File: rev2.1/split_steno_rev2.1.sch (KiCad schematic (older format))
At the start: 59 parts, among them J1 USB_OTG, J2 Audio-Jack-4, J3 Conn_01x03, P1 TC2030-IDC, SW1 SW_Push, SW10 SW_Push, SW11 SW_Push, SW12 SW_Push, SW13 SW_Push, SW14 SW_Push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

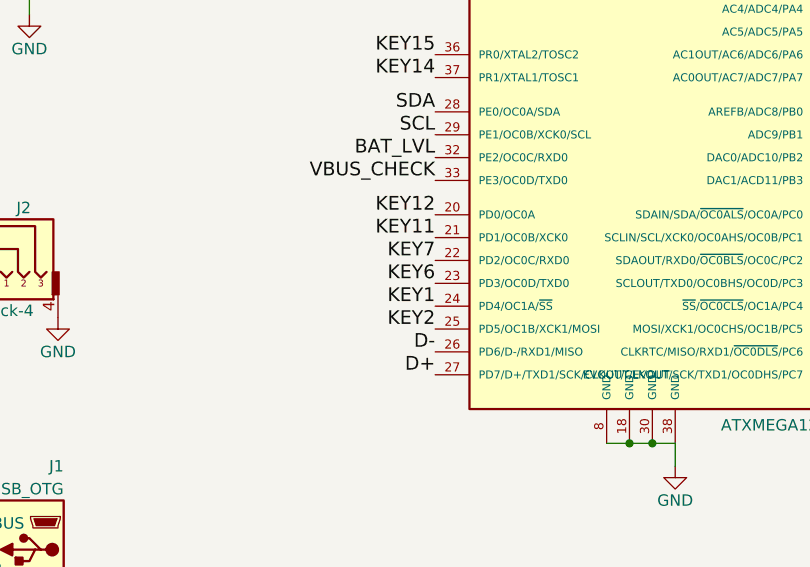
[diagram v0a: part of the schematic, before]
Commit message: routed USB, left side switches
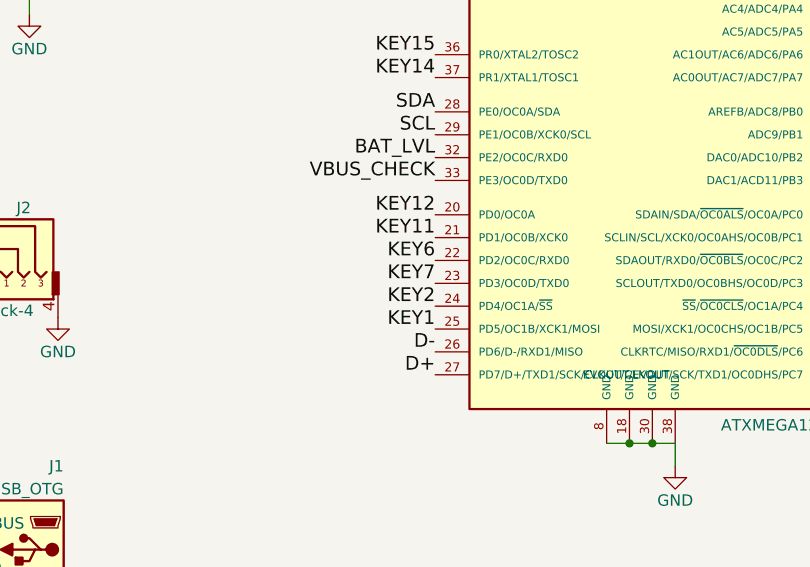
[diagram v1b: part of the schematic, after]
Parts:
- J1: footprint keyboard_parts:USB_miniB -> conn_usb:USB_MicroB_Amphenol_10118194-0001LF
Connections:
- net KEY1: now also U5.25 (PD5/OC1B/XCK1/MOSI); no longer U5.24 (PD4/OC1A/~SS~)
- net KEY2: now also U5.24 (PD4/OC1A/~SS~); no longer U5.25 (PD5/OC1B/XCK1/MOSI)
- net KEY6: now also U5.22 (PD2/OC0C/RXD0); no longer U5.23 (PD3/OC0D/TXD0)
- net KEY7: now also U5.23 (PD3/OC0D/TXD0); no longer U5.22 (PD2/OC0C/RXD0)
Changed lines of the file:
@@
 F 0 "J1" H 6175 7075 50  0000 L CNN
 F 1 "USB_OTG" H 6175 6975 50  0000 L CNN
-F 2 "keyboard_parts:USB_miniB" H 6525 6575 50  0001 C CNN
+F 2 "conn_usb:USB_MicroB_Amphenol_10118194-0001LF" H 6525 6575 50  0001 C CNN
 F 3 "" H 6525 6575 50  0001 C CNN
 	1    6375 6625
@@
 Text Label 8200 5775 2    60   ~ 0
 D+
+Text Label 8200 5575 2    60   ~ 0
+KEY1
 Text Label 8200 5475 2    60   ~ 0
-KEY1
-Text Label 8200 5575 2    60   ~ 0
 KEY2
 Text Label 10000 4725 0    60   ~ 0
@@
 Text Label 10000 4475 0    60   ~ 0
 KEY5
+Text Label 8200 5275 2    60   ~ 0
+KEY6
 Text Label 8200 5375 2    60   ~ 0
-KEY6
-Text Label 8200 5275 2    60   ~ 0
 KEY7
 Text Label 10000 3875 0    60   ~ 0

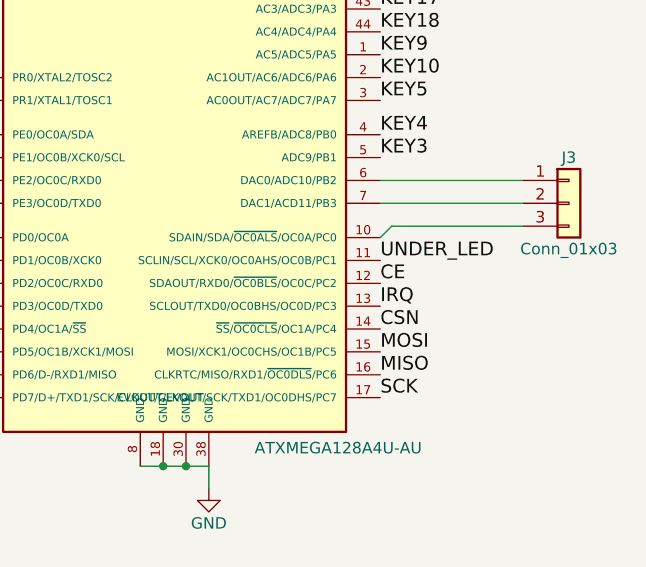
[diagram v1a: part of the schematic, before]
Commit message: rerouted left half
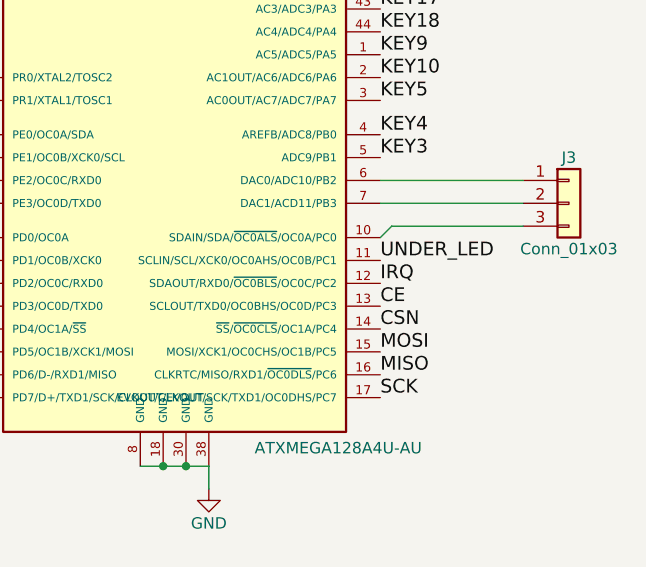
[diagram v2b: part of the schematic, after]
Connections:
- net CE: now also U5.13 (SCLOUT/TXD0/OC0BHS/OC0D/PC3); no longer U5.12 (SDAOUT/RXD0/~OC0BLS~/OC0C/PC2)
- net IRQ: now also U5.12 (SDAOUT/RXD0/~OC0BLS~/OC0C/PC2); no longer U5.13 (SCLOUT/TXD0/OC0BHS/OC0D/PC3)
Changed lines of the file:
@@
 Text Label 10000 5775 0    60   ~ 0
 SCK
+Text Label 10000 5375 0    60   ~ 0
+CE
 Text Label 10000 5275 0    60   ~ 0
-CE
-Text Label 10000 5375 0    60   ~ 0
 IRQ
 $Comp

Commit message: switched from micro to mini b
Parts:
- J1: footprint conn_usb:USB_MicroB_Amphenol_10118194-0001LF -> keyboard_parts:USB_miniB_hirose_5S8
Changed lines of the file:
@@
 F 0 "J1" H 6175 7075 50  0000 L CNN
 F 1 "USB_OTG" H 6175 6975 50  0000 L CNN
-F 2 "conn_usb:USB_MicroB_Amphenol_10118194-0001LF" H 6525 6575 50  0001 C CNN
+F 2 "keyboard_parts:USB_miniB_hirose_5S8" H 6525 6575 50  0001 C CNN
 F 3 "" H 6525 6575 50  0001 C CNN
 	1    6375 6625
